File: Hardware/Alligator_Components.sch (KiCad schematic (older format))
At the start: 100 parts, among them J1 SWD_Header, J2 Eurorack_10_pin_power, J3 Conn_01x20_Female, U1 STM32H743ZITx, U2 IS42S16400J-xC, U3 MCP6004, U4 PCM5100APW, U5 TL072, U7 LM1117-3.3, U8 SSI2164, Y1 8MHz 20pF

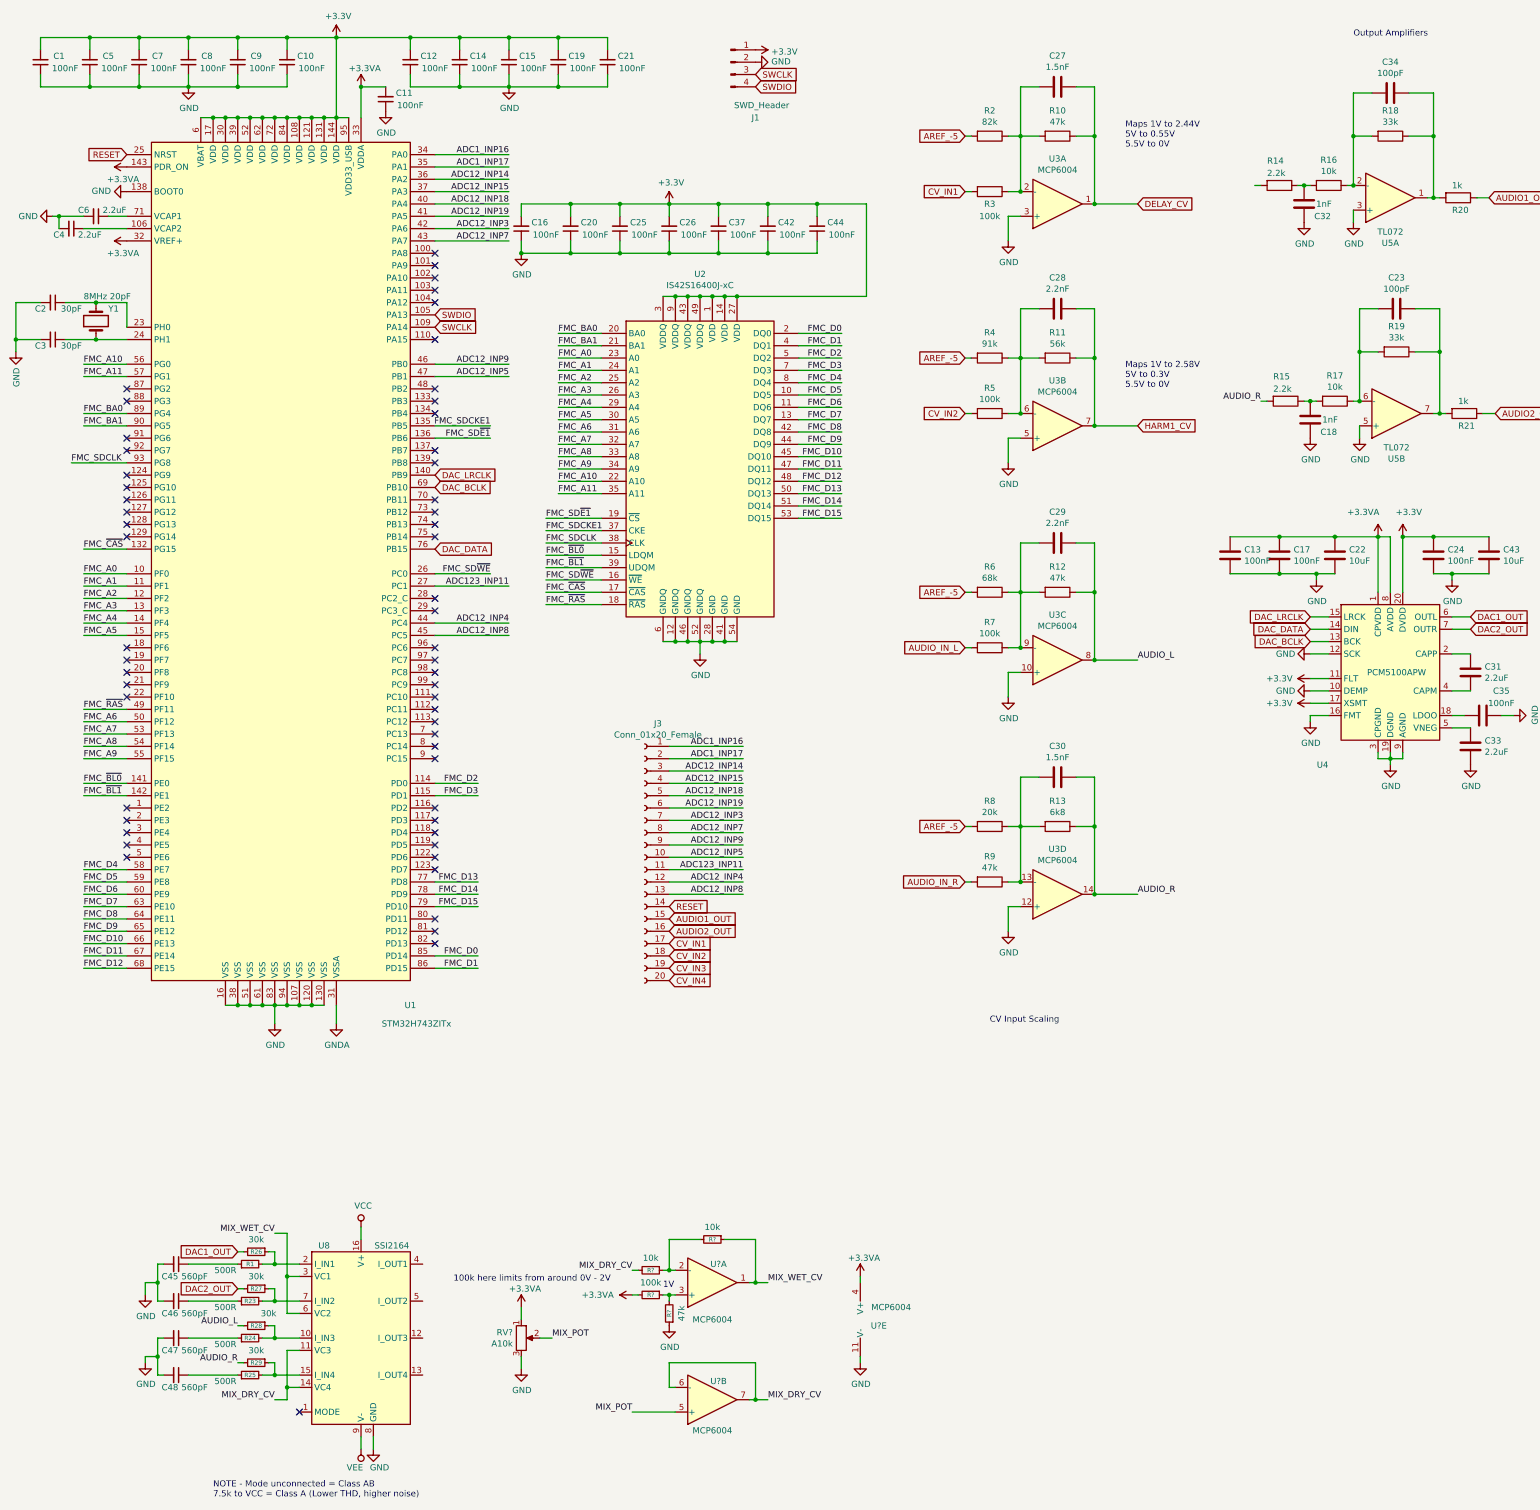
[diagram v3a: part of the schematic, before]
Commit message: Implemented Wet/Dry mix control using MCU to process curves
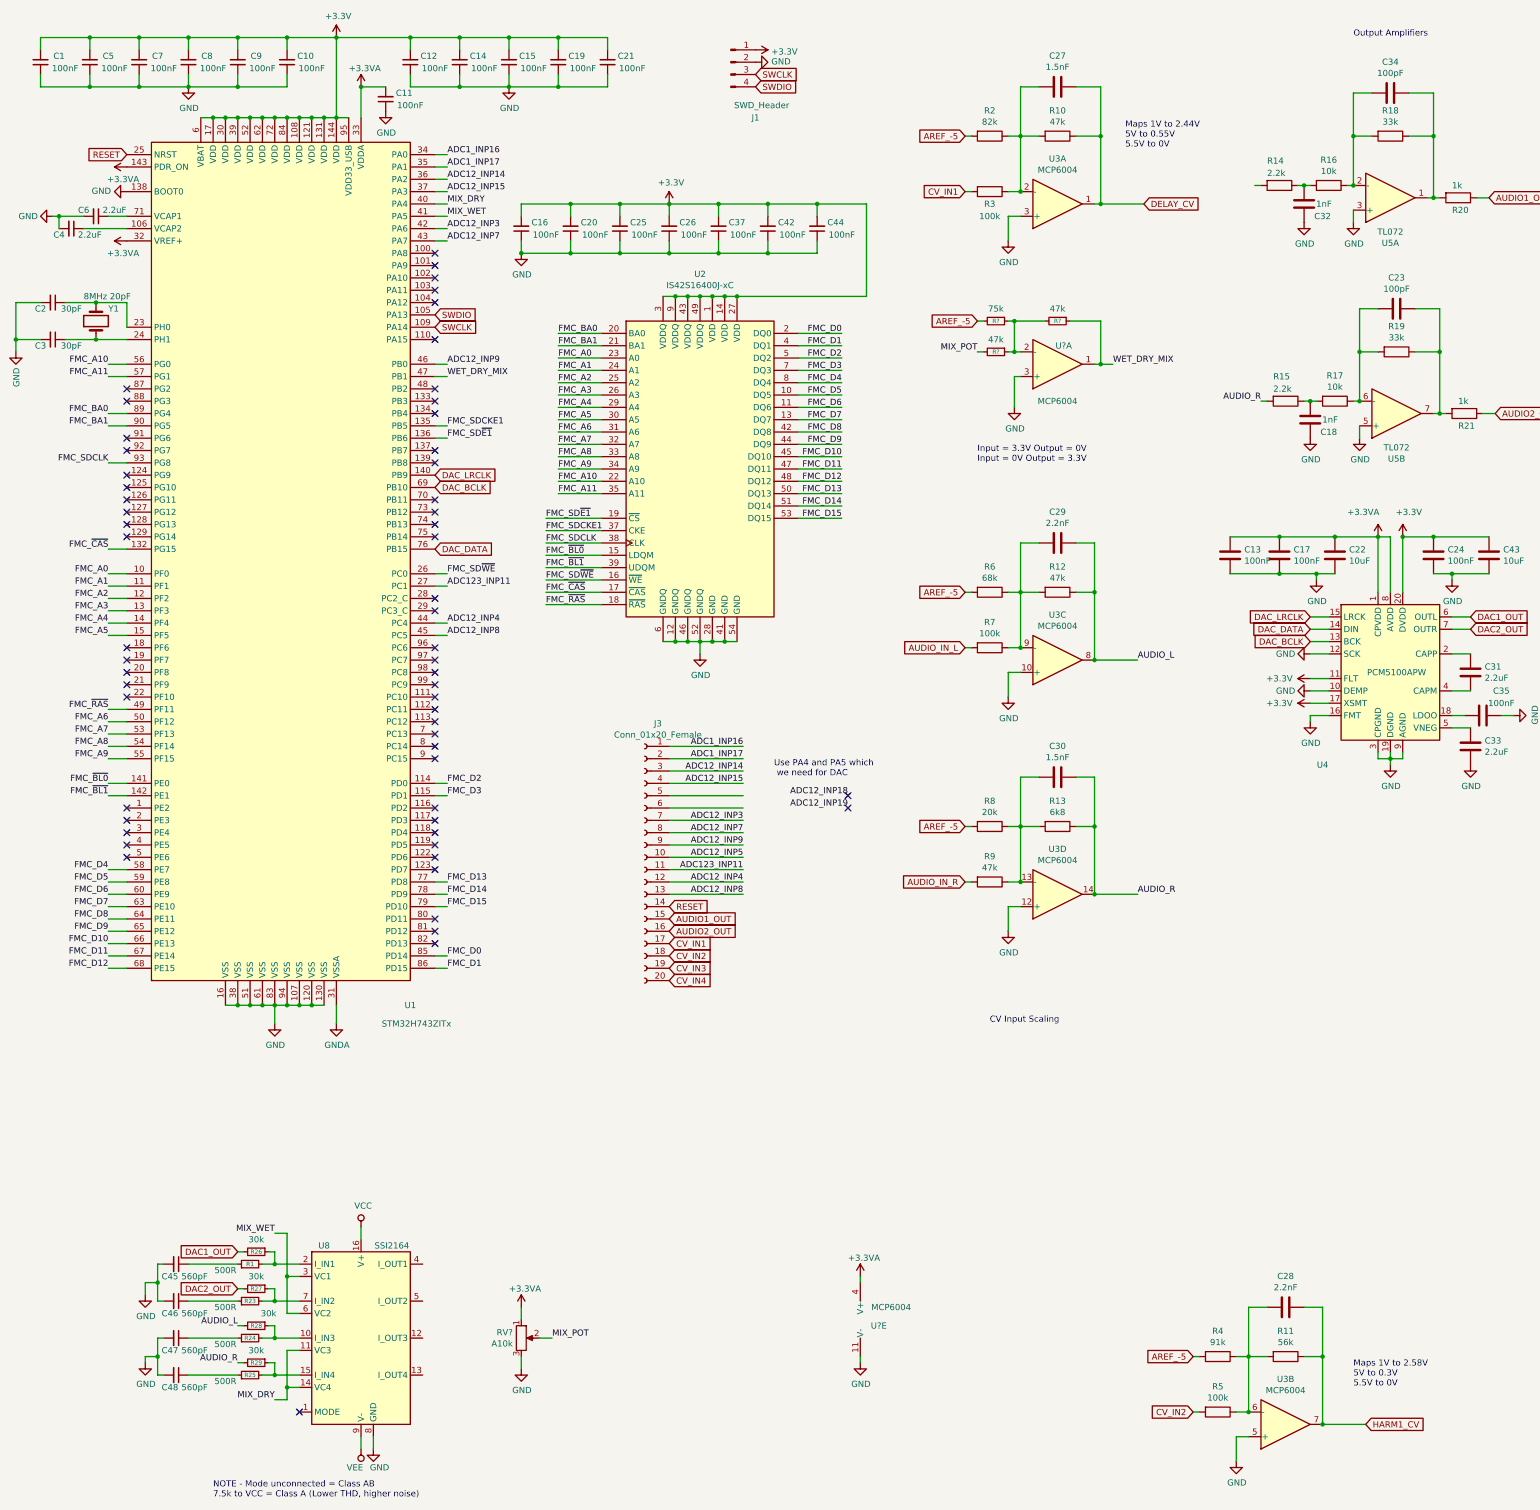
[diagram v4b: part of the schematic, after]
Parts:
- removed R?: 100k, symbol Device:R_Small
- removed R?: 47k, symbol Device:R_Small
- removed U?: MCP6004, SMD_Packages:SOIC-14_N, symbol Amplifier_Operational:MCP6004
- added R?: 75k, symbol Device:R_Small
- R? (x2): value 10k -> 47k
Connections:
- net ADC12_INP18: no longer J3.5 (Pin_5), U1.40 (PA4)
- net ADC12_INP19: no longer J3.6 (Pin_6), U1.41 (PA5)
- net ADC12_INP5: no longer U1.47 (PB1)
- net AREF_-5: now also R?.2
- net GND: now also U?.3 (+)
- net MIX_POT: now also R?.2
- net at R?.1, R?.2, U?.2 (-): now also R?.1
- net MIX_DRY_CV renamed MIX_DRY
- net MIX_DRY: now also U1.40 (PA4); no longer R?.2
- net MIX_WET_CV renamed MIX_WET
- net MIX_WET: now also U1.41 (PA5); no longer R?.1, U?.1
- new net WET_DRY_MIX: R?.1, U1.47 (PB1), U?.1
- no-connect marks 57 -> 59
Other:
- note added: "Input = 3.3V Output = 0V\nInput = 0V Output = 3.3V"
- note added: "Use PA4 and PA5 which\n we need for DAC"
- note removed: "100k here limits from around 0V - 2V"
- note removed: "1V"
- moved on the sheet: C28, R11, R4, R5, R?, U3B, U?A

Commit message: Updates to schematic
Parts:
- removed C18, C32: 1nF, Capacitors_SMD:C_0805_HandSoldering, symbol Device:C
- removed C27: 1.5nF, Capacitors_SMD:C_0805_HandSoldering, symbol Device:C
- removed R10: 47k, Resistors_SMD:R_0805_HandSoldering, symbol Device:R
- removed R14, R15: 2.2k, Resistors_SMD:R_0805_HandSoldering, symbol Device:R
- removed R16, R17: 10k, Resistors_SMD:R_0805_HandSoldering, symbol Device:R
- removed R2: 82k, Resistors_SMD:R_0805_HandSoldering, symbol Device:R
- removed R3: 100k, Resistors_SMD:R_0805_HandSoldering, symbol Device:R
- removed unit 1 of U5
- removed unit 2 of U5
- added C? (x2): 1nF, symbol Device:C_Small
- added C? (x2): 100pF, symbol Device:C_Small
- added C?: 1.5nF, symbol Device:C_Small
- added R?: 91k, symbol Device:R_Small
- added R? (x2): 2k2, symbol Device:R_Small
- added R? (x2): 10k, symbol Device:R_Small
- added R? (x2): 33k, symbol Device:R_Small
- added R? (x2): 1k, symbol Device:R_Small
- added R?: 47k, symbol Device:R_Small
- added R?: 100k, symbol Device:R_Small
- added R?: 68k, symbol Device:R_Small
- added U? (x4): TL074, symbol Amplifier_Operational:TL074
- C29: value 2.2nF -> 1.5nF
- R12: value 47k -> 6k8
- R6: value 68k -> 20k
- R7: value 100k -> 47k
- gave numbers to parts that had none: 1
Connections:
- net ADC123_INP11: now also J3.9 (Pin_9); no longer J3.11 (Pin_11)
- net ADC12_INP3: now also J3.5 (Pin_5); no longer J3.7 (Pin_7)
- net ADC12_INP4: now also J3.10 (Pin_10); no longer J3.12 (Pin_12)
- net ADC12_INP5: now also J3.8 (Pin_8); no longer J3.10 (Pin_10)
- net ADC12_INP7: now also J3.6 (Pin_6); no longer J3.8 (Pin_8)
- net ADC12_INP8: now also J3.11 (Pin_11); no longer J3.13 (Pin_13)
- net ADC12_INP9: now also J3.7 (Pin_7); no longer J3.9 (Pin_9)
- net AREF_-5: now also R?.2
- net AUDIO_IN_L: now also C29.2, R12.1, U3.8; no longer R7.2
- net AUDIO_IN_R: now also C30.2, R13.1, U3.14; no longer R9.2
- net AUDIO_L: no longer C29.2, R12.1, U3.8
- net AUDIO_R: no longer C30.2, R13.1, U3.14
- net DAC1_OUT: no longer U4.6 (OUTL)
- net DAC2_OUT: no longer U4.7 (OUTR)
- net DELAY_CV: now also R?.2; no longer U3.1
- net GND: now also U3.5 (+), C?.2, C?.2, U?.10 (+), U?.12 (+), U?.3 (+), U?.5 (+); no longer U3.3 (+)
- net WET_DRY_MIX: now also U3.7; no longer U3.1
- net at U3.2 (-): now also C?.2, R?.1, R?.1, R?.2
- net at C34.2, R18.1, R20.2: now also U?.1
- net DRY_OUT_L: now reaches C34.1, R18.2
- net DRY_OUT_L: now also U8.12 (I_OUT3), U8.4 (I_OUT1), U?.2 (-)
- net DRY_OUT_R: now reaches U8.13 (I_OUT4)
- net DRY_OUT_R: now also C23.1, R19.2, U8.5 (I_OUT2), U?.6 (-)
- net at C23.2, R19.1, R21.2: now also U?.7
- net at R?.1, R?.1, R?.2: now also U3.6 (-), R?.1; no longer U3.2 (-)
- net AUDIO1_OUT renamed EXT_AUDIO_OUT_L
- net EXT_AUDIO_OUT_L: now also R?.1
- net AUDIO2_OUT renamed EXT_AUDIO_OUT_R
- net EXT_AUDIO_OUT_R: now also R?.1
- new net: C?.1, R?.1, R?.2, U?.8
- new net: C?.2, R?.1, R?.2, U?.9 (-)
- new net: C?.1, R?.1, R?.2 (x2)
- new net: C?.2, R?.1, R?.2, U?.13 (-)
- new net: C?.1, R?.1, R?.2, U?.14
- new net DAC_OUT_L: R?.2, U4.6 (OUTL)
- new net DAC_OUT_R: R?.2, U4.7 (OUTR)
- new net DELAY_CV_SCALED: C?.1, R?.1, U3.1
- new net EXT_AUDIO_IN_L: J3.12 (Pin_12), R7.2
- new net EXT_AUDIO_IN_R: J3.13 (Pin_13), R9.2
- new net MIX_CV: R?.2
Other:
- note added: "Full Scale: 7V"
- note added: "Output Buffers"
- note added: "POT Full scale: 3.3V \nCV Full scale: 6.4V"
- note added: "Wet Output Amplifiers"
- note removed: "Input = 3.3V Output = 0V\nInput = 0V Output = 3.3V"
- note removed: "Maps 1V to 2.44V\n5V to 0.55V\n5.5V to 0V"
- note removed: "Output Amplifiers"
- moved on the sheet: C23, C34, R18, R19, R21, R?, RV?

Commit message: Added remaining Opamp blocks to schematic and started control design
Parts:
- removed C23, C34: 100pF, Capacitors_SMD:C_0805_HandSoldering, symbol Device:C
- removed C28: 2.2nF, Capacitors_SMD:C_0805_HandSoldering, symbol Device:C
- removed C29, C30: 1.5nF, Capacitors_SMD:C_0805_HandSoldering, symbol Device:C
- removed C45, C46, C47, C48: 560pF, symbol Device:C_Small
- removed C?: 1nF, symbol Device:C_Small
- removed C?: 100pF, symbol Device:C_Small
- removed R1, R23, R24, R25: 500R, symbol Device:R_Small
- removed R26, R27, R28, R29: 30k, symbol Device:R_Small
- removed R?: 91k, symbol Device:R_Small
- removed R?: 75k, symbol Device:R_Small
- removed R? (x3): 47k, symbol Device:R_Small
- removed R? (x2): 2k2, symbol Device:R_Small
- removed R? (x2): 10k, symbol Device:R_Small
- removed R? (x2): 33k, symbol Device:R_Small
- removed R? (x2): 1k, symbol Device:R_Small
- removed R?: 100k, symbol Device:R_Small
- removed R?: 68k, symbol Device:R_Small
- removed U5: TL072, SMD_Packages:SOIC-8-N, symbol Amplifier_Operational:TL072
- removed U?: TL074, symbol Amplifier_Operational:TL074
- added C?: 1nF, symbol Device:C_Small
- added C? (x3): 100pF, symbol Device:C_Small
- added C? (x5): 1.5nF, symbol Device:C_Small
- added C? (x4): 560pF, symbol Device:C_Small
- added R? (x4): 47k, Resistors_SMD:R_0805_HandSoldering, symbol Device:R
- added R?: 75k, Resistors_SMD:R_0805_HandSoldering, symbol Device:R
- added R? (x2): 91k, Resistors_SMD:R_0805_HandSoldering, symbol Device:R
- added R? (x2): 68k, Resistors_SMD:R_0805_HandSoldering, symbol Device:R
- added R? (x3): 100k, Resistors_SMD:R_0805_HandSoldering, symbol Device:R
- added R? (x2): 33k, Resistors_SMD:R_0805_HandSoldering, symbol Device:R
- added R? (x2): 10k, Resistors_SMD:R_0805_HandSoldering, symbol Device:R
- added R? (x2): 2k2, Resistors_SMD:R_0805_HandSoldering, symbol Device:R
- added R? (x2): 1k, Resistors_SMD:R_0805_HandSoldering, symbol Device:R
- added R?: 56k, Resistors_SMD:R_0805_HandSoldering, symbol Device:R
- added R? (x4): 30k, symbol Device:R_Small
- added R? (x4): 500R, symbol Device:R_Small
- added SW?: SW_SPST, symbol Switch:SW_SPST
- added SW?: SW_SPDT_MSM, symbol Switch:SW_SPDT_MSM
- added SW?: SW_Push, symbol Switch:SW_Push
- added unit 4 of U5
- added U6 (x2): MCP6004, SMD_Packages:SOIC-14_N, symbol Amplifier_Operational:MCP6004
- added unit 5 of U7
- added U?: TL074, symbol Amplifier_Operational:TL074
- C13, C17, C22, C24, C31, C33, C35, C43: symbol Device:C -> Device:C_Small
- R18, R19: value 33k -> 30k
- gave numbers to parts that had none: 2
- renumbered U4 to U3, U8 to U4, U3 to U5, U3 to U6, U7 to U8
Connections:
- net AREF_-5: now also R?.2, R?.2, R?.2, R?.2
- net AUDIO_IN_L: now also U5.1, C?.1; no longer U5.8
- net AUDIO_IN_R: now also U5.7, C?.1; no longer U5.14
- net AUDIO_L: now also R?.2
- net AUDIO_R: now also R?.2
- net DAC_OUT_L: now also R?.2
- net DAC_OUT_R: now also R?.2
- net DRY_OUT_L: now also C?.2
- net DRY_OUT_R: now also C?.2
- net GND: now also U5.10 (+), U5.3 (+), U5.5 (+), U6.3 (+), C?.2, C?.2, C?.2, C?.2, C?.2, SW?.1, U5.12 (+), U6.5 (+), U?.12 (+); no longer U5.10 (+), U5.12 (+), U5.3 (+), U6.5 (+)
- net MIX_CV: now also R?.2
- net MIX_POT: now also R?.2
- net SWCLK: now also J1.4 (Pin_4); no longer J1.3 (Pin_3)
- net VCC: now also U7.11 (V-)
- net VEE: now also U7.4 (V+)
- net WET_DRY_MIX: now also U6.1, R?.1; no longer U6.7
- net at C?.2: now also U5.9 (-), R?.1, R?.1, R?.2; no longer U5.2 (-)
- net at R11.2, R4.1, R5.1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: now also C?.2
- net at R12.2, R6.1, R7.1: now also U5.2 (-), C?.2; no longer U5.9 (-)
- net at R13.2, R8.1, R9.1: now also U5.6 (-), C?.2; no longer U5.13 (-)
- net at R18.1, R20.2, U7.1: now also C?.1
- net at U4.10 (I_IN3): now also R?.1, R?.2
- net at U4.15 (I_IN4): now also R?.1, R?.2
- net at U4.2 (I_IN1): now also R?.1, R?.2
- net at U4.7 (I_IN2): now also R?.1, R?.2
- net at R19.1, R21.2, U?.7: now also C?.1
- net at C?.1, U?.8: now also R?.1, R?.2
- net at C?.2, U?.9 (-): now also R?.1, R?.2
- net at C?.1: now also R?.1, R?.2
- net CV_IN1: no longer names the net of J3.17 (Pin_17)
- net CV_IN2: no longer names the net of J3.18 (Pin_18)
- net CV_IN2: no longer R5.2
- net CV_IN3: no longer names the net of J3.19 (Pin_19)
- net CV_IN4: no longer names the net of J3.20 (Pin_20)
- net DELAY_CV_SCALED renamed DELAY_CV_SCALED_L
- net DELAY_CV_SCALED_L: now also U5.8, R?.1; no longer U5.1
- net HARM1_CV renamed FEEDBACK_CV_SCALED
- net FEEDBACK_CV_SCALED: now also C?.1
- net SWDIO renamed SWIO
- net SWIO: now also J1.3 (Pin_3); no longer J1.4 (Pin_4)
- new net: R?.1, R?.1, R?.1, R?.2, U6.2 (-)
- new net: C?.2, R?.1, R?.2, U?.13 (-)
- new net: C?.1, R?.1, R?.2, U?.14
- new net: C?.1, R?.1, R?.2
- new net: C?.2, R?.1, R?.1, R?.2, U5.13 (-)
- new net: C?.2, R?.1, R?.1, R?.2, U6.6 (-)
- new net: C?.1, R?.1, U6.7
- new net: C?.1, R?.1 (x4)
- new net CLOCK: U6.5 (+)
- new net CLOCK_SCALED: U6.6 (-), U6.7
- new net DAC_OUT_AMP_L: R?.1, R?.2
- new net DAC_OUT_AMP_R: R?.1, R?.2
- new net DELAY_CV_L: R?.2
- new net DELAY_CV_R: R?.2
- new net DELAY_CV_SCALED_R: C?.1, R?.1, U5.14
- new net FEEDBACK_CV: R5.2
- new net MODE_BTN: SW?.2
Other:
- note removed: "Maps 1V to 2.58V\n5V to 0.3V\n5.5V to 0V"
- moved on the sheet: C11, C13, C16, C17, C20, C22, C24, C25, C26, C31, C33, C35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
